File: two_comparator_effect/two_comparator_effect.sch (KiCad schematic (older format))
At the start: 29 parts, among them J1 RCA, J2 RCA, J3 Barrel_Jack, Q1 2N3904, U1 LM339, U2 LM317

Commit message: revised all boards
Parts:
- J1, J2: value RCA -> rca; footprint lib_fp:RCJ-024 -> lib_fp:tht_rca_vertical
- RV1, RV2: value 1k -> 1k_pot
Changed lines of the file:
@@
 Connection ~ 2550 6400
-$Comp
-L Connector:Conn_Coaxial J1
-U 1 1 5EB59891
-P 2350 4050
-F 0 "J1" H 2278 4288 50  0000 C CNN
-F 1 "RCA" H 2278 4197 50  0000 C CNN
-F 2 "lib_fp:RCJ-024" H 2350 4050 50  0001 C CNN
-F 3 " ~" H 2350 4050 50  0001 C CNN
-	1    2350 4050
-	-1   0    0    -1
-$EndComp
 $Comp
 L power:GND #PWR013
@@
 P 4300 2950
 F 0 "RV2" H 4230 2996 50  0000 R CNN
-F 1 "1k" H 4230 2905 50  0000 R CNN
+F 1 "1k_pot" H 4230 2905 50  0000 R CNN
 F 2 "lib_fp:Potentiometer_Vertical_Large" H 4300 2950 50  0001 C CNN
 F 3 "~" H 4300 2950 50  0001 C CNN
@@
 P 8900 4350
 F 0 "J2" H 9000 4325 50  0000 L CNN
-F 1 "RCA" H 9000 4234 50  0000 L CNN
-F 2 "lib_fp:RCJ-024" H 8900 4350 50  0001 C CNN
+F 1 "rca" H 9000 4234 50  0000 L CNN
+F 2 "lib_fp:tht_rca_vertical" H 8900 4350 50  0001 C CNN
 F 3 " ~" H 8900 4350 50  0001 C CNN
 	1    8900 4350
@@
 P 3500 1650
 F 0 "RV1" H 3430 1696 50  0000 R CNN
-F 1 "1k" H 3430 1605 50  0000 R CNN
+F 1 "1k_pot" H 3430 1605 50  0000 R CNN
 F 2 "lib_fp:Potentiometer_Vertical_Large" H 3500 1650 50  0001 C CNN
 F 3 "~" H 3500 1650 50  0001 C CNN
@@
 Wire Wire Line
 	7725 4350 7725 4475
+$Comp
+L Connector:Conn_Coaxial J1
+U 1 1 5EB59891
+P 2350 4050
+F 0 "J1" H 2278 4288 50  0000 C CNN
+F 1 "rca" H 2278 4197 50  0000 C CNN
+F 2 "lib_fp:tht_rca_vertical" H 2350 4050 50  0001 C CNN
+F 3 " ~" H 2350 4050 50  0001 C CNN
+	1    2350 4050
+	-1   0    0    -1
+$EndComp
 $EndSCHEMATC

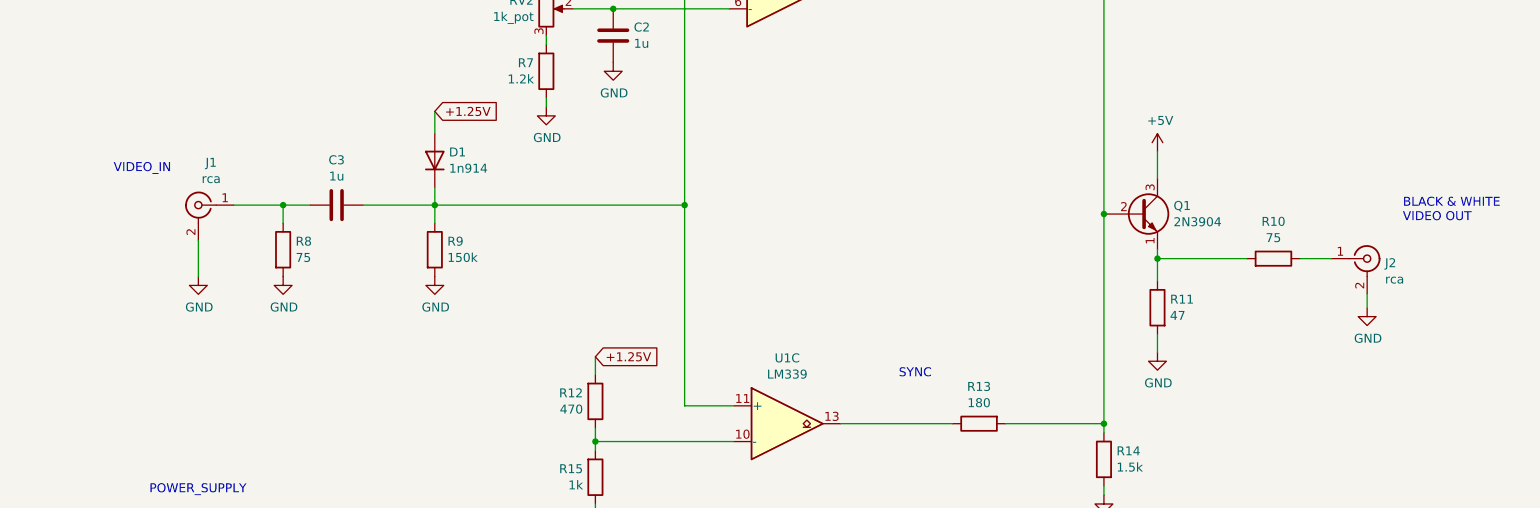
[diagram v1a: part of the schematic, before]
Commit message: update for new chroma_luma circuit
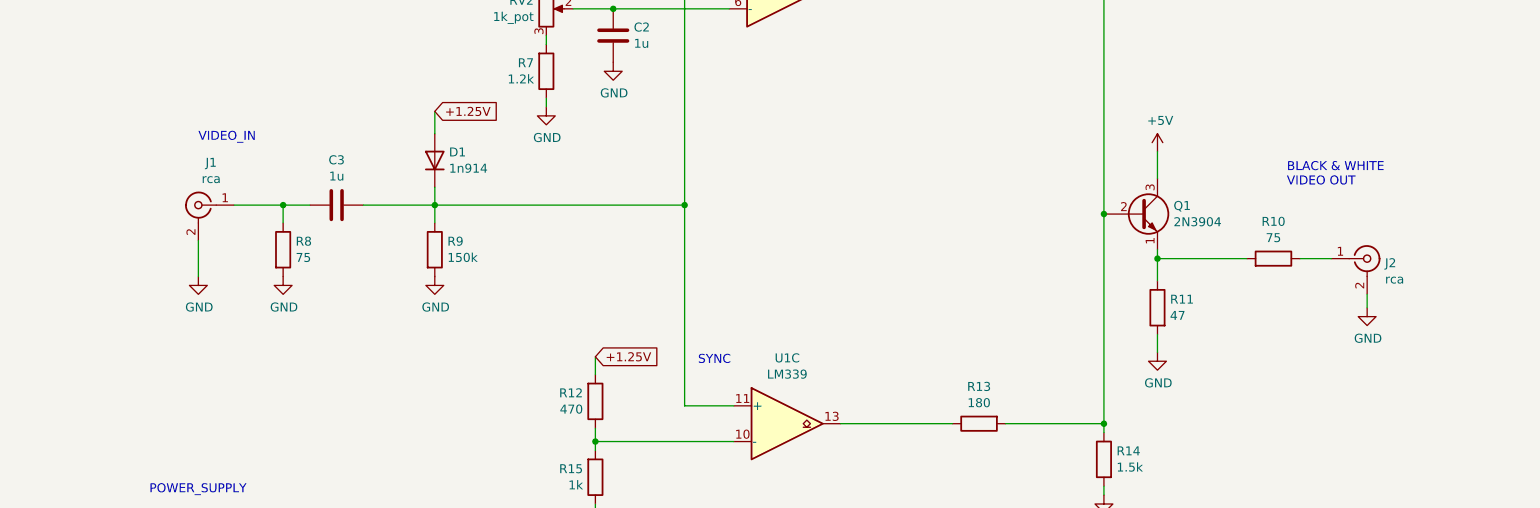
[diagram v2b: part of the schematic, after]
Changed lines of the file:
@@
 EESchema Schematic File Version 4
-LIBS:two_comparator_effect-cache
 EELAYER 30 0
 EELAYER END
@@
 Wire Wire Line
 	5925 2850 6475 2850
-Text Notes 6275 5025 0    50   ~ 0
+Text Notes 5150 4950 0    50   ~ 0
 SYNC
 $Comp
@@
 Wire Wire Line
 	8900 4550 8900 4625
-Text Notes 1875 3875 0    50   ~ 0
+Text Notes 2350 3700 0    50   ~ 0
 VIDEO_IN
-Text Notes 9100 4150 0    50   ~ 0
+Text Notes 8450 3950 0    50   ~ 0
 BLACK & WHITE \nVIDEO OUT
 Text Notes 3600 2775 0    50   ~ 0

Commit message: newest circuit revisions
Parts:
- added SW1: SW_DPDT_x2, lib:dpdt_mini_toggle_switch_tayda, symbol Switch:SW_DPDT_x2
- J1, J2: footprint lib_fp:tht_rca_vertical -> lib:tht_rca_vertical
- RV1, RV2: footprint lib_fp:Potentiometer_Vertical_Large -> lib:Potentiometer_Vertical_Large
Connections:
- net video_in: now reaches C3.2, R8.1
- net video_in: now also SW1.3 (C); no longer J1.1 (In)
- net at J2.1 (In): now also SW1.5 (B); no longer R10.1
- new net: J1.1 (In), SW1.2 (B)
- new net: SW1.1 (A), SW1.4 (A)
- new net video_out: R10.1, SW1.6 (C)
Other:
- note added: "SIGNAL_BYBASS"
- moved on the sheet: J1, J2, J3, R16, U2
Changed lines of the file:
@@
 L Regulator_Linear:LM317_3PinPackage U2
 U 1 1 5EB5729E
-P 2550 6100
-F 0 "U2" H 2550 6342 50  0000 C CNN
-F 1 "LM317" H 2550 6251 50  0000 C CNN
-F 2 "Package_TO_SOT_THT:TO-92_HandSolder" H 2550 6325 50  0001 C CIN
-F 3 "http://www.ti.com/lit/ds/snvs775k/snvs775k.pdf" H 2550 6100 50  0001 C CNN
-	1    2550 6100
+P 1950 7000
+F 0 "U2" H 1950 7242 50  0000 C CNN
+F 1 "LM317" H 1950 7151 50  0000 C CNN
+F 2 "Package_TO_SOT_THT:TO-92_HandSolder" H 1950 7225 50  0001 C CIN
+F 3 "http://www.ti.com/lit/ds/snvs775k/snvs775k.pdf" H 1950 7000 50  0001 C CNN
+	1    1950 7000
 	1    0    0    -1
 $EndComp
@@
 L power:GND #PWR023
 U 1 1 5EB57A13
-P 2550 6500
-F 0 "#PWR023" H 2550 6250 50  0001 C CNN
-F 1 "GND" H 2555 6327 50  0000 C CNN
-F 2 "" H 2550 6500 50  0001 C CNN
-F 3 "" H 2550 6500 50  0001 C CNN
-	1    2550 6500
-	1    0    0    -1
-$EndComp
-Wire Wire Line
-	2550 6400 2550 6500
+P 1950 7400
+F 0 "#PWR023" H 1950 7150 50  0001 C CNN
+F 1 "GND" H 1955 7227 50  0000 C CNN
+F 2 "" H 1950 7400 50  0001 C CNN
+F 3 "" H 1950 7400 50  0001 C CNN
+	1    1950 7400
+	1    0    0    -1
+$EndComp
+Wire Wire Line
+	1950 7300 1950 7400
 $Comp
 L power:+5V #PWR019
 U 1 1 5EB58912
-P 2025 5975
-F 0 "#PWR019" H 2025 5825 50  0001 C CNN
-F 1 "+5V" H 2040 6148 50  0000 C CNN
-F 2 "" H 2025 5975 50  0001 C CNN
-F 3 "" H 2025 5975 50  0001 C CNN
-	1    2025 5975
-	1    0    0    -1
-$EndComp
-Wire Wire Line
-	2025 5975 2025 6100
-Wire Wire Line
-	2025 6100 2175 6100
-Text GLabel 3100 5925 2    50   Input ~ 0
+P 1425 6875
+F 0 "#PWR019" H 1425 6725 50  0001 C CNN
+F 1 "+5V" H 1440 7048 50  0000 C CNN
+F 2 "" H 1425 6875 50  0001 C CNN
+F 3 "" H 1425 6875 50  0001 C CNN
+	1    1425 6875
+	1    0    0    -1
+$EndComp
+Wire Wire Line
+	1425 6875 1425 7000
+Wire Wire Line
+	1425 7000 1575 7000
+Text GLabel 2500 6825 2    50   Input ~ 0
 +1.25V
 Wire Wire Line
-	2850 6100 3100 6100
-Wire Wire Line
-	3100 6100 3100 5925
+	2250 7000 2500 7000
+Wire Wire Line
+	2500 7000 2500 6825
 $Comp
 L Device:R R16
 U 1 1 5EB5929E
-P 3100 6250
-F 0 "R16" H 3170 6296 50  0000 L CNN
-F 1 "100" H 3170 6205 50  0000 L CNN
-F 2 "Resistor_THT:R_Axial_DIN0207_L6.3mm_D2.5mm_P7.62mm_Horizontal" V 3030 6250 50  0001 C CNN
-F 3 "~" H 3100 6250 50  0001 C CNN
-	1    3100 6250
-	1    0    0    -1
-$EndComp
-Connection ~ 3100 6100
-Wire Wire Line
-	3100 6400 2550 6400
-Connection ~ 2550 6400
+P 2500 7150
+F 0 "R16" H 2570 7196 50  0000 L CNN
+F 1 "100" H 2570 7105 50  0000 L CNN
+F 2 "Resistor_THT:R_Axial_DIN0207_L6.3mm_D2.5mm_P7.62mm_Horizontal" V 2430 7150 50  0001 C CNN
+F 3 "~" H 2500 7150 50  0001 C CNN
+	1    2500 7150
+	1    0    0    -1
+$EndComp
+Connection ~ 2500 7000
+Wire Wire Line
+	2500 7300 1950 7300
+Connection ~ 1950 7300
 $Comp
 L power:GND #PWR013
 U 1 1 5EB5A54D
-P 2350 4450
-F 0 "#PWR013" H 2350 4200 50  0001 C CNN
-F 1 "GND" H 2355 4277 50  0000 C CNN
-F 2 "" H 2350 4450 50  0001 C CNN
-F 3 "" H 2350 4450 50  0001 C CNN
-	1    2350 4450
+P 850 5600
+F 0 "#PWR013" H 850 5350 50  0001 C CNN
+F 1 "GND" H 855 5427 50  0000 C CNN
+F 2 "" H 850 5600 50  0001 C CNN
+F 3 "" H 850 5600 50  0001 C CNN
+	1    850  5600
 	1    0    0    -1
 $EndComp
@@
 $EndComp
 Wire Wire Line
-	2550 4050 2825 4050
-Wire Wire Line
-	2350 4250 2350 4450
-Wire Wire Line
 	2825 4150 2825 4050
-Connection ~ 2825 4050
-Wire Wire Line
-	2825 4050 2975 4050
 Wire Wire Line
 	3675 4050 3675 4150
@@
 F 0 "RV2" H 4230 2996 50  0000 R CNN
 F 1 "1k_pot" H 4230 2905 50  0000 R CNN
-F 2 "lib_fp:Potentiometer_Vertical_Large" H 4300 2950 50  0001 C CNN
+F 2 "lib:Potentiometer_Vertical_Large" H 4300 2950 50  0001 C CNN
 F 3 "~" H 4300 2950 50  0001 C CNN
 	1    4300 2950
@@
 L Connector:Conn_Coaxial J2
 U 1 1 5EBAE02B
-P 8900 4350
-F 0 "J2" H 9000 4325 50  0000 L CNN
-F 1 "rca" H 9000 4234 50  0000 L CNN
-F 2 "lib_fp:tht_rca_vertical" H 8900 4350 50  0001 C CNN
-F 3 " ~" H 8900 4350 50  0001 C CNN
-	1    8900 4350
-	1    0    0    -1
-$EndComp
-Wire Wire Line
-	8525 4350 8700 4350
+P 850 5950
+F 0 "J2" H 950 5925 50  0000 L CNN
+F 1 "rca" H 950 5834 50  0000 L CNN
+F 2 "lib:tht_rca_vertical" H 850 5950 50  0001 C CNN
+F 3 " ~" H 850 5950 50  0001 C CNN
+	1    850  5950
+	-1   0    0    -1
+$EndComp
 $Comp
 L power:GND #PWR016
 U 1 1 5EBB0C30
-P 8900 4625
-F 0 "#PWR016" H 8900 4375 50  0001 C CNN
-F 1 "GND" H 8905 4452 50  0000 C CNN
-F 2 "" H 8900 4625 50  0001 C CNN
-F 3 "" H 8900 4625 50  0001 C CNN
-	1    8900 4625
-	1    0    0    -1
-$EndComp
-Wire Wire Line
-	8900 4550 8900 4625
+P 850 6150
+F 0 "#PWR016" H 850 5900 50  0001 C CNN
+F 1 "GND" H 855 5977 50  0000 C CNN
+F 2 "" H 850 6150 50  0001 C CNN
+F 3 "" H 850 6150 50  0001 C CNN
+	1    850  6150
+	1    0    0    -1
+$EndComp
 Text Notes 2350 3700 0    50   ~ 0
 VIDEO_IN
@@
 F 0 "RV1" H 3430 1696 50  0000 R CNN
 F 1 "1k_pot" H 3430 1605 50  0000 R CNN
-F 2 "lib_fp:Potentiometer_Vertical_Large" H 3500 1650 50  0001 C CNN
+F 2 "lib:Potentiometer_Vertical_Large" H 3500 1650 50  0001 C CNN
 F 3 "~" H 3500 1650 50  0001 C CNN
 	1    3500 1650
@@
 L power:PWR_FLAG #FLG0101
 U 1 1 5EE5DD74
-P 2175 6125
-F 0 "#FLG0101" H 2175 6200 50  0001 C CNN
-F 1 "PWR_FLAG" V 2175 6252 50  0000 L CNN
-F 2 "" H 2175 6125 50  0001 C CNN
-F 3 "~" H 2175 6125 50  0001 C CNN
-	1    2175 6125
+P 1575 7025
+F 0 "#FLG0101" H 1575 7100 50  0001 C CNN
+F 1 "PWR_FLAG" V 1575 7152 50  0000 L CNN
+F 2 "" H 1575 7025 50  0001 C CNN
+F 3 "~" H 1575 7025 50  0001 C CNN
+	1    1575 7025
 	-1   0    0    1
 $EndComp
@@
 L Connector:Barrel_Jack_Switch J3
 U 1 1 5EE8590E
-P 1525 6200
-F 0 "J3" H 1582 6517 50  0000 C CNN
-F 1 "Barrel_Jack" H 1582 6426 50  0000 C CNN
-F 2 "Connector_BarrelJack:BarrelJack_Horizontal" H 1575 6160 50  0001 C CNN
-F 3 "~" H 1575 6160 50  0001 C CNN
-	1    1525 6200
+P 925 7100
+F 0 "J3" H 982 7417 50  0000 C CNN
+F 1 "Barrel_Jack" H 982 7326 50  0000 C CNN
+F 2 "Connector_BarrelJack:BarrelJack_Horizontal" H 975 7060 50  0001 C CNN
+F 3 "~" H 975 7060 50  0001 C CNN
+	1    925  7100
 	1    0    0    -1
 $EndComp
@@
 L power:GND #PWR024
 U 1 1 5EE88B2A
-P 1925 6500
-F 0 "#PWR024" H 1925 6250 50  0001 C CNN
-F 1 "GND" H 1930 6327 50  0000 C CNN
-F 2 "" H 1925 6500 50  0001 C CNN
-F 3 "" H 1925 6500 50  0001 C CNN
-	1    1925 6500
-	1    0    0    -1
-$EndComp
-Wire Wire Line
-	1825 6200 1925 6200
-Wire Wire Line
-	1925 6200 1925 6300
-Wire Wire Line
-	1825 6300 1925 6300
-Connection ~ 1925 6300
-Wire Wire Line
-	1925 6300 1925 6500
-Wire Wire Line
-	1825 6100 2025 6100
-Connection ~ 2025 6100
-Wire Wire Line
-	2175 6125 2175 6100
-Connection ~ 2175 6100
-Wire Wire Line
-	2175 6100 2250 6100
-Text Notes 2075 5675 0    50   ~ 0
+P 1325 7400
+F 0 "#PWR024" H 1325 7150 50  0001 C CNN
+F 1 "GND" H 1330 7227 50  0000 C CNN
+F 2 "" H 1325 7400 50  0001 C CNN
+F 3 "" H 1325 7400 50  0001 C CNN
+	1    1325 7400
+	1    0    0    -1
+$EndComp
+Wire Wire Line
+	1225 7100 1325 7100
+Wire Wire Line
+	1325 7100 1325 7200
+Wire Wire Line
+	1225 7200 1325 7200
+Connection ~ 1325 7200
+Wire Wire Line
+	1325 7200 1325 7400
+Wire Wire Line
+	1225 7000 1425 7000
+Connection ~ 1425 7000
+Wire Wire Line
+	1575 7025 1575 7000
+Connection ~ 1575 7000
+Wire Wire Line
+	1575 7000 1650 7000
+Text Notes 1475 6575 0    50   ~ 0
 POWER_SUPPLY
 $Comp
@@
 L Connector:Conn_Coaxial J1
 U 1 1 5EB59891
-P 2350 4050
-F 0 "J1" H 2278 4288 50  0000 C CNN
-F 1 "rca" H 2278 4197 50  0000 C CNN
-F 2 "lib_fp:tht_rca_vertical" H 2350 4050 50  0001 C CNN
-F 3 " ~" H 2350 4050 50  0001 C CNN
-	1    2350 4050
+P 850 5400
+F 0 "J1" H 778 5638 50  0000 C CNN
+F 1 "rca" H 778 5547 50  0000 C CNN
+F 2 "lib:tht_rca_vertical" H 850 5400 50  0001 C CNN
+F 3 " ~" H 850 5400 50  0001 C CNN
+	1    850  5400
 	-1   0    0    -1
 $EndComp
+$Comp
+L Switch:SW_DPDT_x2 SW1
+U 1 1 6173B2E6
+P 1600 5400
+F 0 "SW1" H 1600 5685 50  0000 C CNN
+F 1 "SW_DPDT_x2" H 1600 5594 50  0000 C CNN
+F 2 "lib:dpdt_mini_toggle_switch_tayda" H 1600 5400 50  0001 C CNN
+F 3 "~" H 1600 5400 50  0001 C CNN
+	1    1600 5400
+	1    0    0    -1
+$EndComp
+$Comp
+L Switch:SW_DPDT_x2 SW1
+U 2 1 6173BAD5
+P 1600 5950
+F 0 "SW1" H 1600 6235 50  0000 C CNN
+F 1 "SW_DPDT_x2" H 1600 6144 50  0000 C CNN
+F 2 "lib:dpdt_mini_toggle_switch_tayda" H 1600 5950 50  0001 C CNN
+F 3 "~" H 1600 5950 50  0001 C CNN
+	2    1600 5950
+	1    0    0    -1
+$EndComp
+Wire Wire Line
+	1050 5400 1400 5400
+Wire Wire Line
+	1050 5950 1400 5950
+Text GLabel 2050 5500 2    50   Input ~ 0
+video_in
+Text GLabel 2450 4050 0    50   Input ~ 0
+video_in
+Wire Wire Line
+	2450 4050 2825 4050
+Connection ~ 2825 4050
+Wire Wire Line
+	2825 4050 2975 4050
+Text GLabel 2050 6050 2    50   Input ~ 0
+video_out
+Wire Wire Line
+	2050 6050 1800 6050
+Wire Wire Line
+	1800 5500 2050 5500
+Wire Wire Line
+	1800 5300 2600 5300
+Wire Wire Line
+	2600 5300 2600 5850
+Wire Wire Line
+	2600 5850 1800 5850
+Text GLabel 8800 4350 2    50   Input ~ 0
+video_out
+Wire Wire Line
+	8525 4350 8800 4350
+Text Notes 1300 5000 0    50   ~ 0
+SIGNAL_BYBASS
 $EndSCHEMATC
